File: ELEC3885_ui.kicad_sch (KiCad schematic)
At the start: 57 parts, among them SW10 SW_Push, SW11 SW_Push, SW12 SW_Push, SW5 SW_Push, SW6 SW_Push, SW7 SW_Push, SW8 SW_Push, SW9 SW_Push, U4 74HC595, U5 74HC595, U6 74HC595

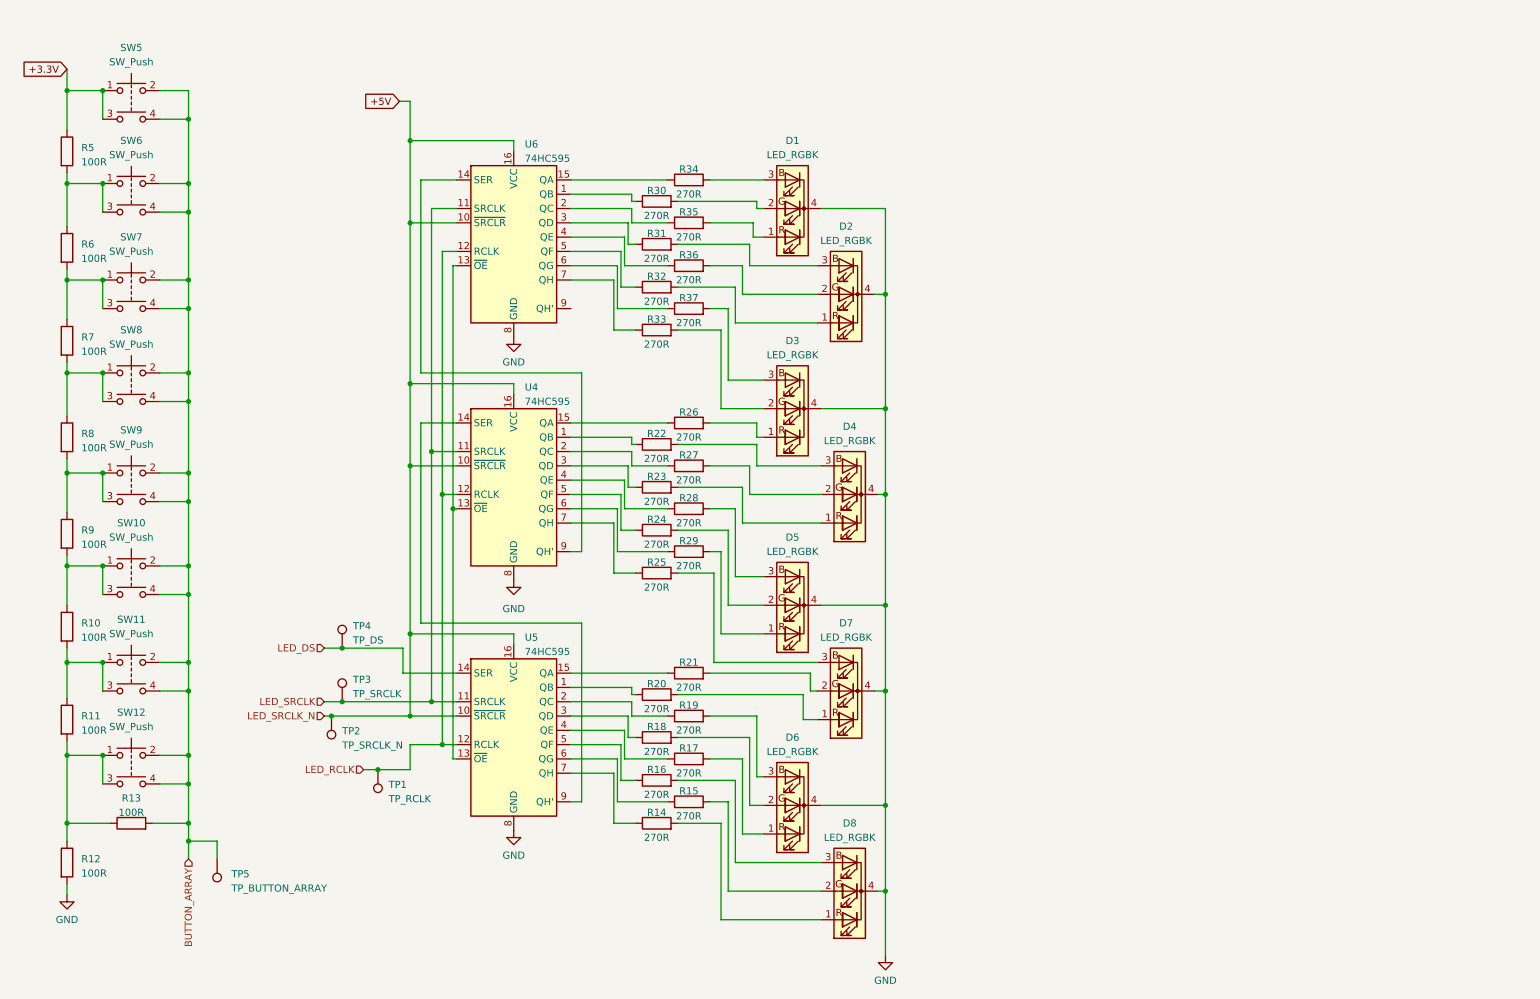
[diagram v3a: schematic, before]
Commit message: Rev3 PCB layout started
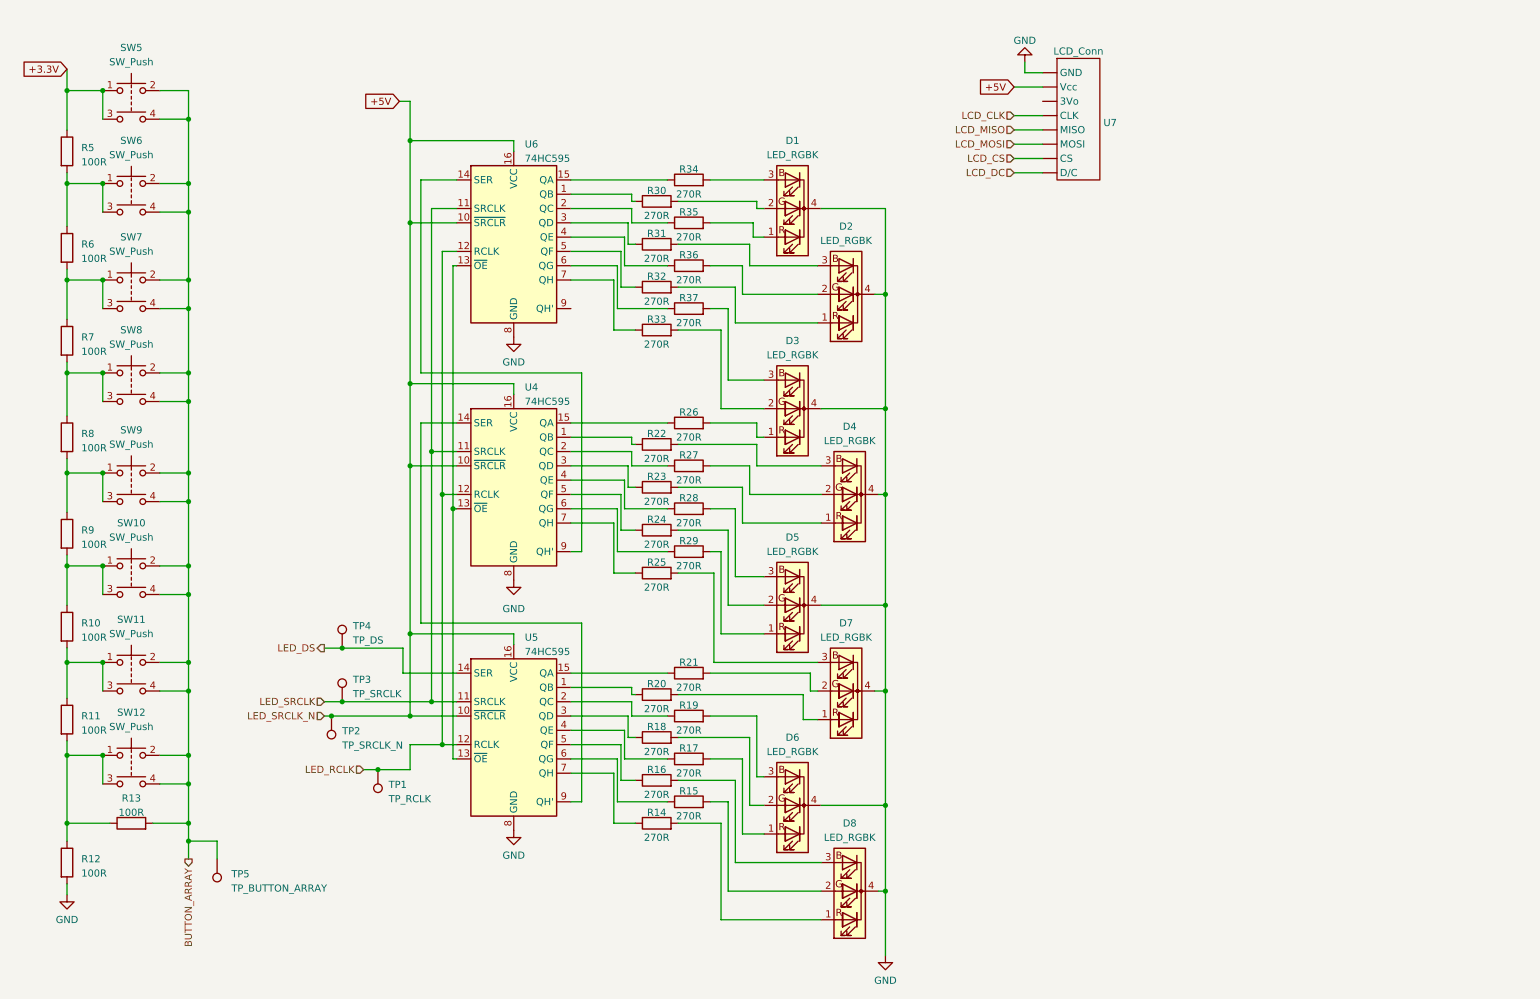
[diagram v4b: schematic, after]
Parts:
- added U7: LCD_Conn, symbol Luke_library:Adafruit_3.5_TFT_SPI
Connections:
- net +5V: now also U7. (Vcc)
- net GND: now also U7. (Vcc)
- new net LCD_CLK: U7. (Vcc)
- new net LCD_CS: U7. (Vcc)
- new net LCD_DC: U7. (Vcc)
- new net LCD_MISO: U7. (Vcc)
- new net LCD_MOSI: U7. (Vcc)
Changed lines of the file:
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@@
+    (stroke (width 0) (type default))
+  )
+  (wire (pts (xy 195.58 24.765) (xy 195.58 26.67))
     (stroke (width 0) (type default))
   )
@@
     (stroke (width 0) (type default))
   )
+  (wire (pts (xy 193.675 41.91) (xy 198.755 41.91))
+    (stroke (width 0) (type default))
+  )
   (wire (pts (xy 114.935 146.05) (xy 123.825 146.05))
     (stroke (width 0) (type default))
@@
     (stroke (width 0) (type default))
   )
+  (wire (pts (xy 193.675 36.83) (xy 198.755 36.83))
+    (stroke (width 0) (type default))
+  )
   (wire (pts (xy 46.99 85.09) (xy 41.91 85.09))
     (stroke (width 0) (type default))
@@
     (stroke (width 0) (type default))
   )
+  (wire (pts (xy 193.675 29.21) (xy 198.755 29.21))
+    (stroke (width 0) (type default))
+  )
   (wire (pts (xy 86.36 96.52) (xy 94.615 96.52))
     (stroke (width 0) (type default))
@@
     (stroke (width 0) (type default))
   )
+  (wire (pts (xy 193.675 39.37) (xy 198.755 39.37))
+    (stroke (width 0) (type default))
+  )
   (wire (pts (xy 94.615 58.42) (xy 92.075 58.42))
     (stroke (width 0) (type default))
@@
     (stroke (width 0) (type default))
   )
+  (wire (pts (xy 193.675 34.29) (xy 198.755 34.29))
+    (stroke (width 0) (type default))
+  )
   (wire (pts (xy 144.145 104.14) (xy 144.145 116.205))
     (stroke (width 0) (type default))
@@
     (stroke (width 0) (type default))
   )
+  (wire (pts (xy 195.58 26.67) (xy 198.755 26.67))
+    (stroke (width 0) (type default))
+  )
   (wire (pts (xy 133.985 137.16) (xy 156.21 137.16))
     (stroke (width 0) (type default))
@@
   )
   (wire (pts (xy 114.935 96.52) (xy 125.095 96.52))
+    (stroke (width 0) (type default))
+  )
+  (wire (pts (xy 193.675 44.45) (xy 198.755 44.45))
     (stroke (width 0) (type default))
   )
@@
     )
   )
+  (global_label "+5V" (shape input) (at 193.675 29.21 180) (fields_autoplaced)
+    (effects (font (size 1.27 1.27)) (justify right))
+    (property "Intersheetrefs" "${INTERSHEET_REFS}" (at 186.8987 29.21 0)
+      (effects (font (size 1.27 1.27)) (justify right) hide)
+    )
+  )
   (global_label "+3.3V" (shape input) (at 25.4 26.035 180) (fields_autoplaced)
     (effects (font (size 1.27 1.27)) (justify right))
@@
     )
   )
-  (hierarchical_label "BUTTON_ARRAY" (shape input) (at 46.99 166.37 270) (fields_autoplaced)
+  (hierarchical_label "BUTTON_ARRAY" (shape output) (at 46.99 166.37 270) (fields_autoplaced)
+    (effects (font (size 1.27 1.27)) (justify right))
+  )
+  (hierarchical_label "LCD_CLK" (shape input) (at 193.675 34.29 180) (fields_autoplaced)
+    (effects (font (size 1.27 1.27)) (justify right))
+  )
+  (hierarchical_label "LCD_DC" (shape input) (at 193.675 44.45 180) (fields_autoplaced)
+    (effects (font (size 1.27 1.27)) (justify right))
+  )
+  (hierarchical_label "LCD_CS" (shape input) (at 193.675 41.91 180) (fields_autoplaced)
+    (effects (font (size 1.27 1.27)) (justify right))
+  )
+  (hierarchical_label "LCD_MISO" (shape input) (at 193.675 36.83 180) (fields_autoplaced)
     (effects (font (size 1.27 1.27)) (justify right))
   )
@@
     (effects (font (size 1.27 1.27)) (justify right))
   )
+  (hierarchical_label "LCD_MOSI" (shape input) (at 193.675 39.37 180) (fields_autoplaced)
+    (effects (font (size 1.27 1.27)) (justify right))
+  )
   (hierarchical_label "LED_SRCLK_N" (shape input) (at 71.12 140.97 180) (fields_autoplaced)
     (effects (font (size 1.27 1.27)) (justify right))
   )
-  (hierarchical_label "LED_DS" (shape input) (at 71.12 128.905 180) (fields_autoplaced)
+  (hierarchical_label "LED_DS" (shape output) (at 71.12 128.905 180) (fields_autoplaced)
     (effects (font (size 1.27 1.27)) (justify right))
   )
@@
         (path "/eaef1172-3351-417c-bfc4-74a598f141cb/edb4d620-a826-41be-bd87-be038303d2ba"
           (reference "R7") (unit 1)
+        )
+      )
+    )
+  )
+  (symbol (lib_name "GND_5") (lib_id "power:GND") (at 195.58 24.765 180) (unit 1)
+    (in_bom yes) (on_board yes) (dnp no) (fields_autoplaced)
+    (property "Reference" "#PWR022" (at 195.58 18.415 0)
+      (effects (font (size 1.27 1.27)) hide)
+    )
+    (property "Value" "GND" (at 195.58 20.955 0)
+      (effects (font (size 1.27 1.27)))
+    )
+    (property "Footprint" "" (at 195.58 24.765 0)
+      (effects (font (size 1.27 1.27)) hide)
+    )
+    (property "Datasheet" "" (at 195.58 24.765 0)
+      (effects (font (size 1.27 1.27)) hide)
+    )
+    (pin "1")
+    (instances
+      (project "ELEC3885"
+        (path "/eaef1172-3351-417c-bfc4-74a598f141cb/edb4d620-a826-41be-bd87-be038303d2ba"
+          (reference "#PWR022") (unit 1)
         )
       )
@@
         )
       )
+    )
+  )
+  (symbol (lib_id "Luke_library:Adafruit_3.5_TFT_SPI") (at 205.105 22.86 0) (unit 1)
+    (in_bom yes) (on_board yes) (dnp no) (fields_autoplaced)
+    (property "Reference" "U7" (at 209.55 35.56 0)
+      (effects (font (size 1.27 1.27)) (justify left))
+    )
+    (property "Value" "LCD_Conn" (at 205.105 22.86 0)
+      (effects (font (size 1.27 1.27)))
+    )
+    (property "Footprint" "" (at 205.105 22.86 0)
+      (effects (font (size 1.27 1.27)) hide)
+    )
+    (property "Datasheet" "" (at 205.105 22.86 0)
+      (effects (font (size 1.27 1.27)) hide)
+    )
+    (pin "")
+    (pin "")
+    (pin "")
+    (pin "")
+    (pin "")
+    (pin "")
+    (pin "")
+    (pin "")
+    (instances
+      (project "ELEC3885"
+        (path "/eaef1172-3351-417c-bfc4-74a598f141cb/edb4d620-a826-41be-bd87-be038303d2ba"
+          (reference "U7") (unit 1)
+        )
+      )

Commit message: Rev3 rework, diff amp jumpers added
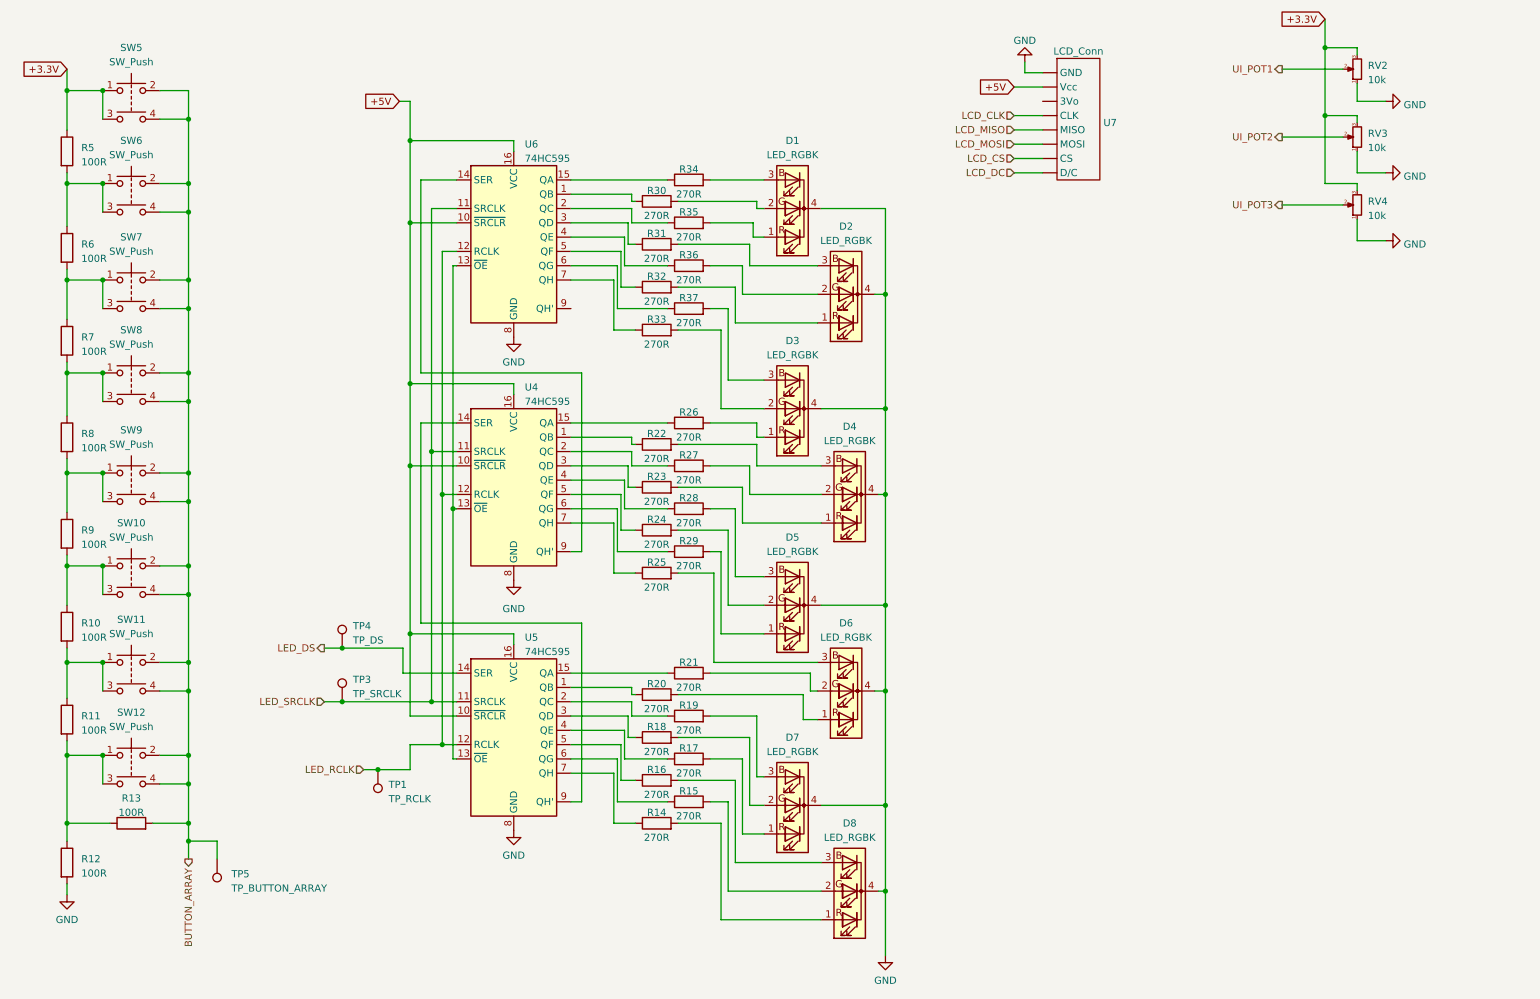
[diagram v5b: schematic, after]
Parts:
- removed TP2: TP_SRCLK_N, symbol Connector:TestPoint
- added RV2, RV3, RV4: 10k, Potentiometer_THT:Potentiometer_Alpha_RD901F-40-00D_Single_Vertical, symbol Device:R_Potentiometer_Small
- D1, D2, D3, D4, D5, D6, D7, D8: footprint (none) -> LED_THT:LED_D5.0mm-4_RGB
- R10, R11, R12, R13, R14, R15, R16, R17, R18, R19, R20, R21, R22, R23, R24, R25, R26, R27, R28, R29, R30, R31, R32, R33, R34, R35, R36, R37, R5, R6, R7, R8, R9: footprint (none) -> Resistor_SMD:R_0402_1005Metric
- TP1, TP3, TP4, TP5: footprint (none) -> TestPoint:TestPoint_Pad_D1.0mm
- U4, U5, U6: footprint (none) -> Package_SO:SOP-16_4.4x10.4mm_P1.27mm
- U7: footprint (none) -> Luke_library:Adafruit_3.5_TFT_SPI
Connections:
- net +3.3V: now also RV2.3, RV3.3, RV4.3
- net GND: now also RV2.1, RV3.1, RV4.1
- net at R21.2: now also D6.2 (GA); no longer D7.2 (GA)
- net at D6.1 (RA): now also R20.2; no longer R17.2
- net at R18.2: now also D7.2 (GA); no longer D6.2 (GA)
- net at D6.3 (BA): now also R25.2; no longer R19.2
- net at D7.3 (BA): now also R19.2; no longer R25.2
- net at D7.1 (RA): now also R17.2; no longer R20.2
- new net UI_POT1: RV2.2
- new net UI_POT2: RV3.2
- new net UI_POT3: RV4.2
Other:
- moved on the sheet: D6, D7

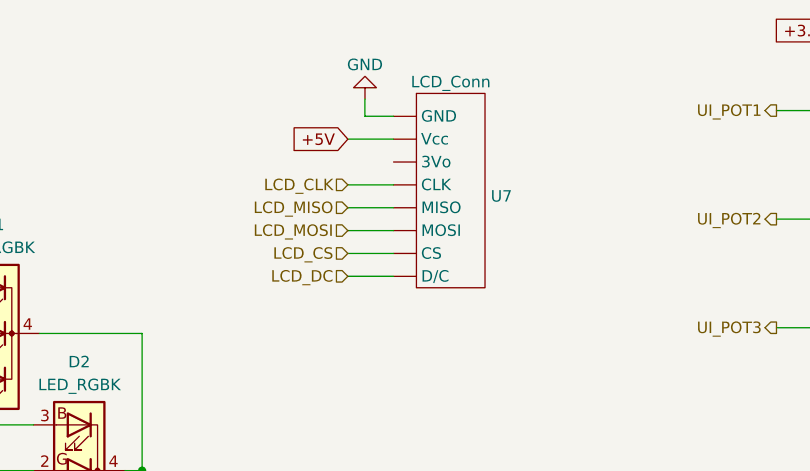
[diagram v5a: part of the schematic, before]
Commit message: LCD footprint fix
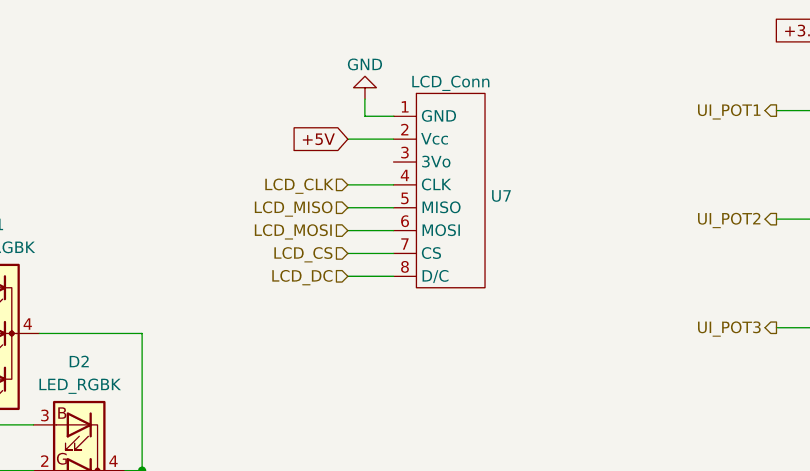
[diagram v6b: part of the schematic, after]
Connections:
- net +5V: now also U7.2 (Vcc); no longer U7. (Vcc)
- net GND: now also U7.1 (GND); no longer U7. (Vcc)
- net LCD_CLK: now also U7.4 (CLK); no longer U7. (Vcc)
- net LCD_CS: now also U7.7 (CS); no longer U7. (Vcc)
- net LCD_DC: now also U7.8 (D/C); no longer U7. (Vcc)
- net LCD_MISO: now also U7.5 (MISO); no longer U7. (Vcc)
- net LCD_MOSI: now also U7.6 (MOSI); no longer U7. (Vcc)
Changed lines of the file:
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@@
       (effects (font (size 1.27 1.27)) hide)
     )
-    (pin "")
-    (pin "")
-    (pin "")
-    (pin "")
-    (pin "")
-    (pin "")
-    (pin "")
-    (pin "")
+    (pin "3")
+    (pin "4")
+    (pin "7")
+    (pin "8")
+    (pin "1")
+    (pin "5")
+    (pin "6")
+    (pin "2")
     (instances
       (project "ELEC3885"
